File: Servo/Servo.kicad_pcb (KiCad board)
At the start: 2 copper layers, 33 x 58.4 mm, 24 parts, among them J1 Pi, J10 Motor2, J11 Conn_01x03, J12 Conn_01x03, J13 Conn_01x03, J14 Conn_01x03, J2 ISP, J3 Power, J4 Conn_01x03, J5 Conn_01x03, J6 Servo 1, J7 Servo 2, J8 Motor1, J9 Laser, U1 ATtiny2313A-PU, U2 L293D

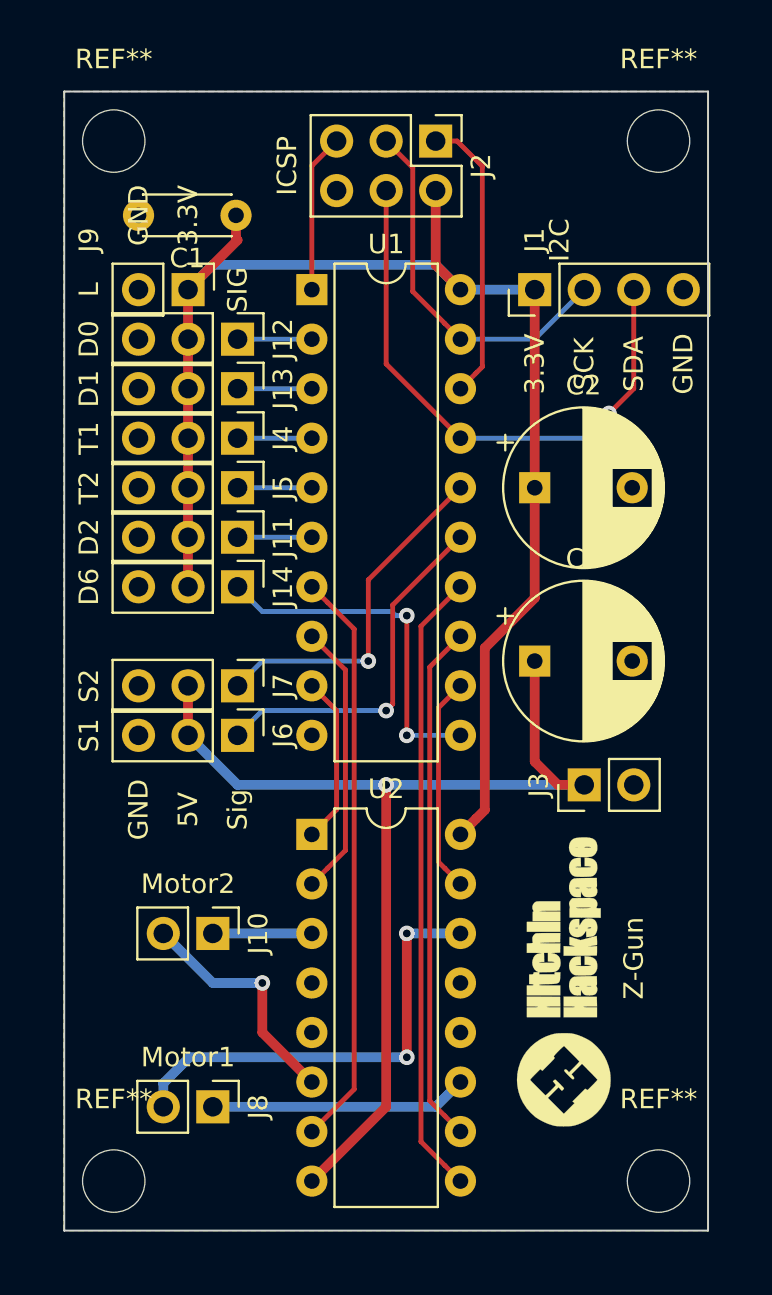
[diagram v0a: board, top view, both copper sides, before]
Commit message: re-factored z-gun code for ease of migration to alternative controllers
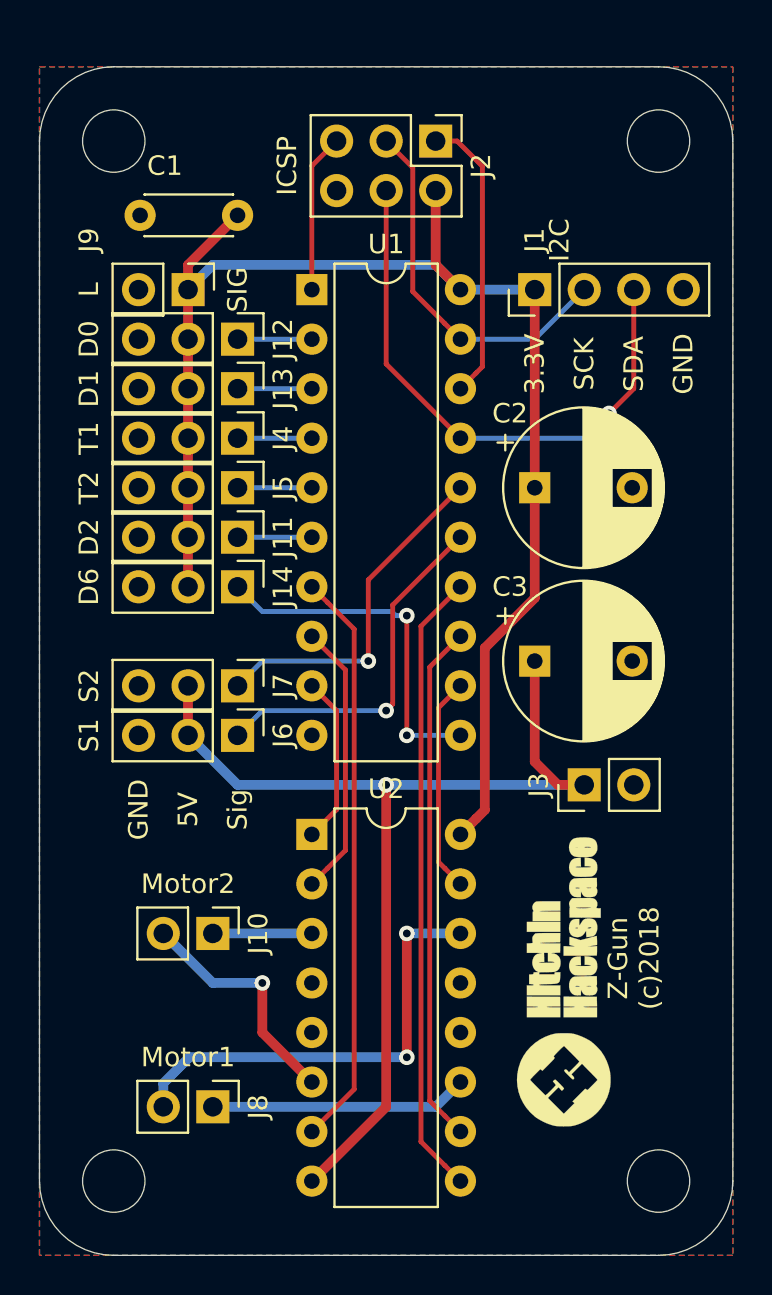
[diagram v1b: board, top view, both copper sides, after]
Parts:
- moved C1 0.08 mm to (106.7, 40.6)
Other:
- board size 33 x 58.4 mm -> 35.6 x 61 mm
- board text added: "Z-Gun (c)2018"
- board text removed: "Z-Gun"
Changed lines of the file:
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@@
   (general
     (thickness 1.6)
-    (drawings 28)
-    (tracks 114)
+    (drawings 30)
+    (tracks 113)
     (zones 0)
     (modules 24)
@@
     (34 B.Paste user hide)
     (35 F.Paste user hide)
-    (36 B.SilkS user hide)
+    (36 B.SilkS user)
     (37 F.SilkS user)
-    (38 B.Mask user hide)
-    (39 F.Mask user hide)
+    (38 B.Mask user)
+    (39 F.Mask user)
     (40 Dwgs.User user hide)
     (41 Cmts.User user hide)
@@
     (43 Eco2.User user hide)
     (44 Edge.Cuts user)
-    (45 Margin user hide)
+    (45 Margin user)
     (46 B.CrtYd user)
-    (47 F.CrtYd user hide)
+    (47 F.CrtYd user)
     (48 B.Fab user hide)
     (49 F.Fab user hide)
@@
     (visible_elements FFFFFF7F)
     (pcbplotparams
-      (layerselection 0x010fc_ffffffff)
+      (layerselection 0x010e0_ffffffff)
       (usegerberextensions false)
       (usegerberattributes false)
@@
       (outputformat 1)
       (mirror false)
-      (drillshape 1)
+      (drillshape 0)
       (scaleselection 1)
-      (outputdirectory ""))
+      (outputdirectory "./"))
   )
   (net 0 "")
@@
     (tags "mounting hole 3.2mm no annular m3")
     (attr virtual)
-    (fp_text reference REF** (at 0 -4.2) (layer F.SilkS)
+    (fp_text reference REF** (at 0 -4.2) (layer F.SilkS) hide
       (effects (font (size 1 1) (thickness 0.15)))
     )
@@
     (tags "mounting hole 3.2mm no annular m3")
     (attr virtual)
-    (fp_text reference REF** (at 0 -4.2) (layer F.SilkS)
+    (fp_text reference REF** (at 0 -4.2) (layer F.SilkS) hide
       (effects (font (size 1 1) (thickness 0.15)))
     )
@@
     (tags "mounting hole 3.2mm no annular m3")
     (attr virtual)
-    (fp_text reference REF** (at 0 -4.2) (layer F.SilkS)
+    (fp_text reference REF** (at 0 -4.2) (layer F.SilkS) hide
       (effects (font (size 1 1) (thickness 0.15)))
     )
@@
     (tags "mounting hole 3.2mm no annular m3")
     (attr virtual)
-    (fp_text reference REF** (at 0 -4.2) (layer F.SilkS)
+    (fp_text reference REF** (at 0 -4.2) (layer F.SilkS) hide
       (effects (font (size 1 1) (thickness 0.15)))
     )
@@
   )
   (module Capacitor_THT:C_Disc_D4.3mm_W1.9mm_P5.00mm (layer F.Cu)
-    (at 106.6 40.64 180)
+    (at 106.68 40.64 180)
     (descr "C, Disc series, Radial, pin pitch=5.00mm, , diameter*width=4.3*1.9mm^2, Capacitor, http://www.vishay.com/docs/45233/krseries.pdf")
     (tags "C Disc series Radial pin pitch 5.00mm  diameter 4.3mm width 1.9mm Capacitor")
-    (fp_text reference C1 (at 2.5 -2.2) (layer F.SilkS)
+    (fp_text reference C1 (at 3.73 2.54) (layer F.SilkS)
       (effects (font (size 1 1) (thickness 0.15)))
     )
@@
     (descr "CP, Radial series, Radial, pin pitch=5.00mm, , diameter=8mm, Electrolytic Capacitor")
     (tags "CP Radial series Radial pin pitch 5.00mm  diameter 8mm Electrolytic Capacitor")
-    (fp_text reference C2 (at 2.5 -5.25) (layer F.SilkS)
+    (fp_text reference C2 (at -1.27 -3.81) (layer F.SilkS)
       (effects (font (size 1 1) (thickness 0.15)))
     )
@@
     (descr "CP, Radial series, Radial, pin pitch=5.00mm, , diameter=8mm, Electrolytic Capacitor")
     (tags "CP Radial series Radial pin pitch 5.00mm  diameter 8mm Electrolytic Capacitor")
-    (fp_text reference C3 (at 2.5 -5.25) (layer F.SilkS)
+    (fp_text reference C3 (at -1.27 -3.81) (layer F.SilkS)
       (effects (font (size 1 1) (thickness 0.15)))
     )
@@
     )
   )
-  (gr_text Z-Gun (at 127 78.74 90) (layer F.SilkS)
+  (gr_line (start 96.52 36.83) (end 96.52 90.17) (layer Edge.Cuts) (width 0.05))
+  (gr_line (start 128.27 33.02) (end 100.33 33.02) (layer Edge.Cuts) (width 0.05))
+  (gr_line (start 132.08 90.17) (end 132.08 36.83) (layer Edge.Cuts) (width 0.05))
+  (gr_line (start 100.33 93.98) (end 128.27 93.98) (layer Edge.Cuts) (width 0.05))
+  (gr_arc (start 100.33 90.17) (end 96.52 90.17) (angle -90) (layer Edge.Cuts) (width 0.05))
+  (gr_arc (start 128.27 90.17) (end 128.27 93.98) (angle -90) (layer Edge.Cuts) (width 0.05))
+  (gr_arc (start 128.27 36.83) (end 132.08 36.83) (angle -90) (layer Edge.Cuts) (width 0.05))
+  (gr_arc (start 100.33 36.83) (end 100.33 33.02) (angle -90) (layer Edge.Cuts) (width 0.05))
+  (gr_text "Z-Gun\n(c)2018" (at 127 78.74 90) (layer F.SilkS)
     (effects (font (size 1 1) (thickness 0.25)))
   )
@@
     (effects (font (size 1 1) (thickness 0.15)))
   )
-  (gr_text GND (at 101.6 40.64 90) (layer F.SilkS)
-    (effects (font (size 1 1) (thickness 0.15)))
-  )
-  (gr_text 3.3V (at 104.14 40.64 90) (layer F.SilkS)
-    (effects (font (size 1 1) (thickness 0.15)))
-  )
   (gr_text ICSP (at 109.22 38.1 90) (layer F.SilkS)
     (effects (font (size 1 1) (thickness 0.15)))
@@
     (effects (font (size 1 1) (thickness 0.15)))
   )
-  (gr_line (start 97.79 92.71) (end 97.79 34.29) (layer Edge.Cuts) (width 0.1))
-  (gr_line (start 130.81 92.71) (end 97.79 92.71) (layer Edge.Cuts) (width 0.1))
-  (gr_line (start 130.81 34.29) (end 130.81 92.71) (layer Edge.Cuts) (width 0.1))
-  (gr_line (start 97.79 34.29) (end 130.81 34.29) (layer Edge.Cuts) (width 0.1))
   (segment (start 106.68 69.85) (end 104.14 67.31) (width 0.5) (layer B.Cu) (net 1) (status 20))
   (segment (start 104.14 64.77) (end 104.14 67.31) (width 0.5) (layer F.Cu) (net 1) (status 30))
@@
   (segment (start 116.84 43.18) (end 105.41 43.18) (width 0.5) (layer B.Cu) (net 2))
   (segment (start 121.92 44.45) (end 121.92 54.61) (width 0.5) (layer F.Cu) (net 2))
-  (segment (start 106.6 41.83) (end 106.6 40.64) (width 0.5) (layer F.Cu) (net 2))
-  (segment (start 104.14 44.45) (end 106.68 41.91) (width 0.5) (layer F.Cu) (net 2))
-  (segment (start 106.68 41.91) (end 106.6 41.83) (width 0.5) (layer F.Cu) (net 2))
   (segment (start 118.909999 71.590001) (end 118.11 72.39) (width 0.5) (layer F.Cu) (net 2))
   (segment (start 119.360001 71.139999) (end 118.909999 71.590001) (width 0.5) (layer F.Cu) (net 2))
@@
   (segment (start 121.92 60.270002) (end 119.360001 62.830001) (width 0.5) (layer F.Cu) (net 2))
   (segment (start 121.92 54.61) (end 121.92 60.270002) (width 0.5) (layer F.Cu) (net 2))
+  (segment (start 106.68 40.64) (end 104.14 43.18) (width 0.5) (layer F.Cu) (net 2))
+  (segment (start 104.14 43.18) (end 104.14 44.45) (width 0.5) (layer F.Cu) (net 2))
   (segment (start 114.3 48.26) (end 118.11 52.07) (width 0.25) (layer F.Cu) (net 4) (status 20))
   (segment (start 114.3 39.37) (end 114.3 48.26) (width 0.25) (layer F.Cu) (net 4) (status 10))
@@
   (segment (start 115.35998 61.17002) (end 114.794295 61.17002) (width 0.25) (layer B.Cu) (net 25))
   (segment (start 114.794295 61.17002) (end 114.584275 60.96) (width 0.25) (layer B.Cu) (net 25))
+  (zone (net 3) (net_name GND) (layer B.Cu) (hatch edge 0.508)
+    (connect_pads (clearance 0.508))
+    (min_thickness 0.254)
+    (fill yes (arc_segments 32) (thermal_gap 0.508) (thermal_bridge_width 0.508))
+    (polygon
+      (pts
+        (xy 96.52 33.02) (xy 132.08 33.02) (xy 132.08 93.98) (xy 96.52 93.98)
+      )
+    )
+  )
   (zone (net 3) (net_name GND) (layer F.Cu) (hatch edge 0.508)
     (connect_pads (clearance 0.508))
@@
     (polygon
       (pts
-        (xy 97.79 34.29) (xy 130.81 34.29) (xy 130.81 92.71) (xy 97.79 92.71)
+        (xy 96.52 33.02) (xy 132.08 33.02) (xy 132.08 93.98) (xy 96.52 93.98)
       )
     )
-  )
-  (zone (net 3) (net_name GND) (layer B.Cu) (hatch edge 0.508)
-    (connect_pads (clearance 0.508))
-    (min_thickness 0.254)
-    (fill yes (arc_segments 32) (thermal_gap 0.508) (thermal_bridge_width 0.508))
-    (polygon
-      (pts
-        (xy 97.79 34.29) (xy 130.81 34.29) (xy 130.81 92.71) (xy 97.79 92.71)
-      )
-    )
